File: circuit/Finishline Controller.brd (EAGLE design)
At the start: 101.6 x 53.3 mm, 8 parts

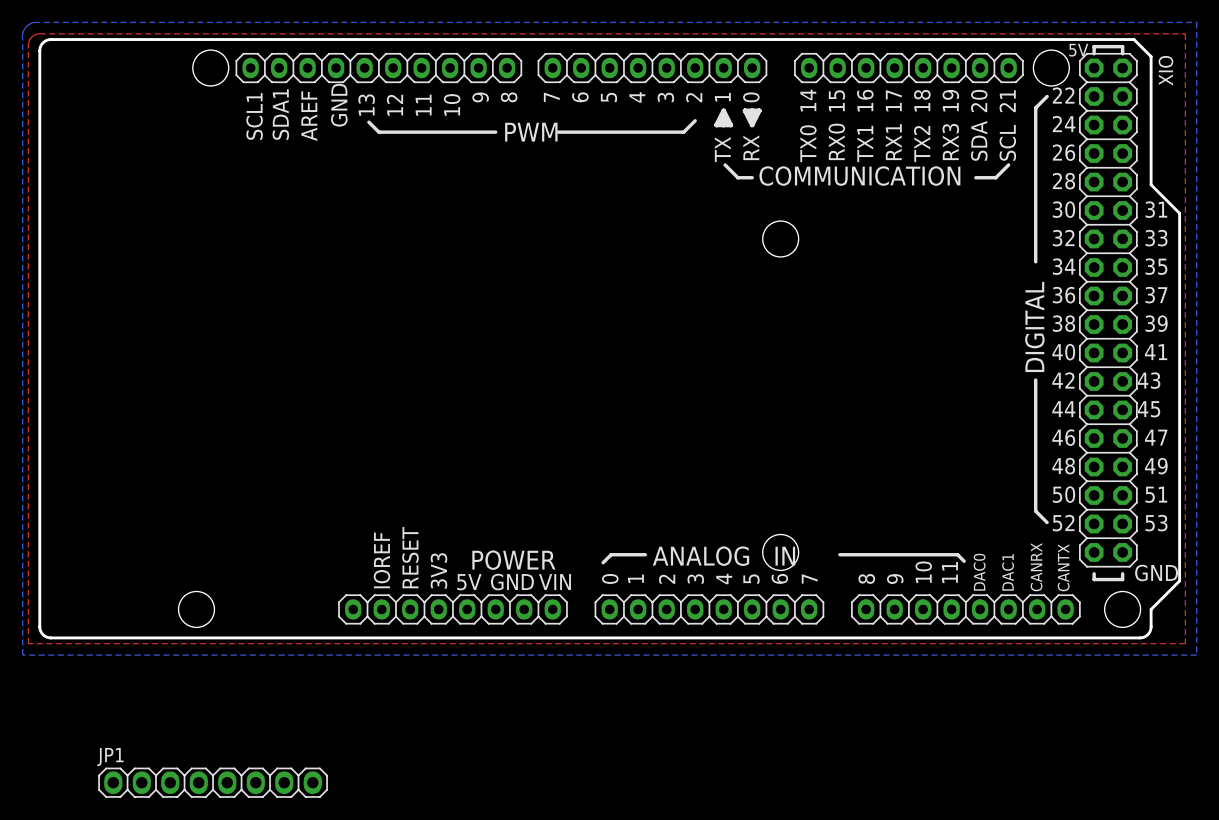
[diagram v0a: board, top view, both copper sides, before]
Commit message: add preliminary Due shield
The Due shield has been populated with all components to drive the
display as well as communicate with the start gate electronics.
A prototyping area with THT and SMD pads has been added as well.
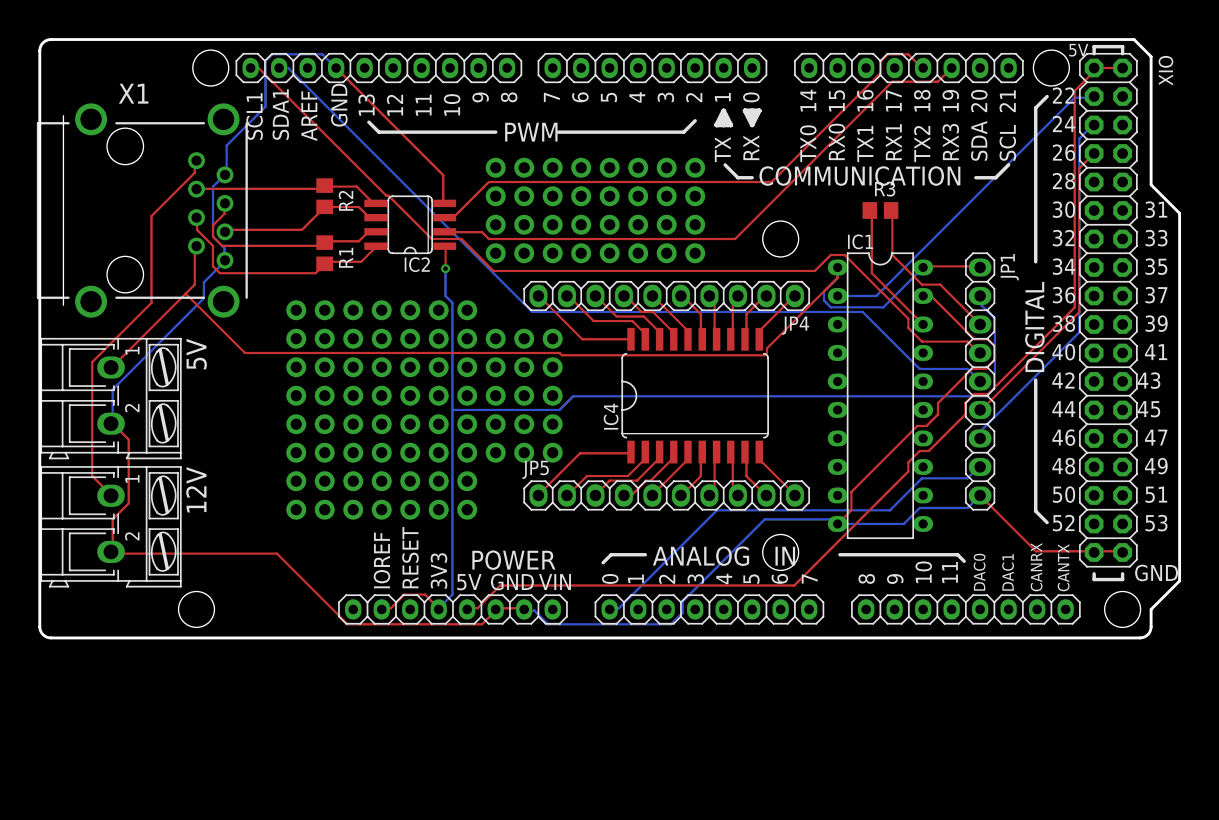
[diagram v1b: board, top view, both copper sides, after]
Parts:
- added 12V: 12V, con-ptr500:AK300/2
- added 5V: 5V, con-ptr500:AK300/2
- added IC1: 74HCT245N, 74xx-eu:DIL20
- added IC2: MAX3490ESA, miro:SO08
- added IC4: 74HCT245DW, 74xx-eu:SO20W
- added JP4, JP5: (no value), pinhead:1X10
- added R1, R2: 120, resistor:R0805
- added R3: 330, resistor:R0805
- added X1: RJ45-6LC21-B, con-tycoelectronics:RJ45-SHIELD1
- JP1: device pinhead:1X08 -> pinhead:1X09
- moved JP1 77.2 mm to (83.8, 22.9), turned to 270 degrees
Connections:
- removed net +3V3: POWER.2, POWER.4
- removed net +5V1: JP1.1
- removed net 0V: JP1.8
- removed net 3.3V: JP1.2
- removed net CLK: JP1.6
- removed net DIO: JP1.7
- removed net SCL: JP1.4
- removed net SDA: JP1.5
- new net +12VEXT: 12V.1, X1.1
- new net +3.3V: IC2.1, JP1.2, POWER.2, POWER.4
- new net +5VEXT: 5V.1, IC1.1, IC1.20, JP1.1, X1.7
- new net N$2: IC1.18, R3.1
- new net N$3: IC2.7, R1.1, X1.4
- new net N$4: IC2.6, R2.2, X1.6
- new net N$5: IC2.5, R2.1, X1.3
- new net N$6: IC2.8, R1.2, X1.5
- new net N$79: IC4.2, JP5.2
- new net N$80: IC4.3, JP5.3
- new net N$81: IC4.4, JP5.4
- new net N$82: IC4.5, JP5.5
- new net N$83: IC4.6, JP5.6
- new net N$84: IC4.7, JP5.7
- new net N$85: IC4.8, JP5.8
- new net N$86: IC4.9, JP5.9
- new net N$87: IC4.10, JP5.10
- new net N$88: IC4.1, JP5.1
- new net N$89: IC4.18, JP4.8
- new net N$90: IC4.17, JP4.7
- new net N$91: IC4.16, JP4.6
- new net N$92: IC4.15, JP4.5
- new net N$93: IC4.14, JP4.4
- new net N$94: IC4.13, JP4.3
- new net N$95: IC4.12, JP4.2
- new net N$96: IC4.11, JP4.1
- new net N$97: IC4.19, JP4.9
- new net N$98: IC4.20, JP4.10
- net AD0: now also JP1.8
- net GND: now also 12V.2, 5V.2, IC1.10, IC1.19, IC2.4, JP1.9, X1.2, X1.8
- net PIN22: now also IC1.2
- net PIN24: now also JP1.7
- net PIN26: now also JP1.6
- net RXD2: now also IC2.2
- net SCL1: now also JP1.4
- net SDA1: now also JP1.5
- net TXD2: now also IC2.3
- net WS2812DATA: now also R3.2
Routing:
- net GND: track 0.00 -> 208.2 mm
- net +5VEXT: track 0.00 -> 97.6 mm
- net +3.3V: track 0.00 -> 97.4 mm, vias 0 -> 1
- net +5V: track 0.00 -> 91.0 mm
- net SCL1: track 0.00 -> 77.2 mm
- net SDA1: track 0.00 -> 74.1 mm
- net RXD2: track 0.00 -> 51.8 mm
- net TXD2: track 0.00 -> 49.8 mm
- net AD0: track 0.00 -> 38.3 mm
- net +12VEXT: track 0.00 -> 34.4 mm
- net PIN24: track 0.00 -> 32.2 mm
- net PIN22: track 0.00 -> 30.2 mm
- net PIN26: track 0.00 -> 27.1 mm
- net N$6: track 0.00 -> 20.9 mm
- net N$3: track 0.00 -> 18.9 mm
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- removed copper zone on layer 1, net GND
- removed copper zone on layer 16, net GND

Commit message: add mounting holes to the Finishline Display board
New PDFs have been added for the display.
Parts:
- renumbered IC4 to PROTOTYPE
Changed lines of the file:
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@@
 <layer number="42" name="bRestrict" color="1" fill="10" visible="yes" active="yes"/>
 <layer number="43" name="vRestrict" color="2" fill="10" visible="yes" active="yes"/>
-<layer number="44" name="Drills" color="7" fill="1" visible="no" active="yes"/>
+<layer number="44" name="Drills" color="7" fill="1" visible="yes" active="yes"/>
 <layer number="45" name="Holes" color="7" fill="1" visible="yes" active="yes"/>
 <layer number="46" name="Milling" color="3" fill="1" visible="no" active="yes"/>
@@
 <layer number="112" name="tSilk" color="7" fill="1" visible="no" active="no"/>
 <layer number="113" name="ReferenceLS" color="7" fill="1" visible="no" active="no"/>
-<layer number="114" name="Badge_Outline" color="7" fill="1" visible="yes" active="yes"/>
-<layer number="115" name="ReferenceISLANDS" color="7" fill="1" visible="yes" active="yes"/>
+<layer number="114" name="Badge_Outline" color="7" fill="1" visible="no" active="yes"/>
+<layer number="115" name="ReferenceISLANDS" color="7" fill="1" visible="no" active="yes"/>
 <layer number="116" name="Patch_BOT" color="7" fill="1" visible="no" active="no"/>
 <layer number="118" name="Rect_Pads" color="7" fill="1" visible="no" active="no"/>
@@
 <layer number="127" name="_tValues" color="7" fill="1" visible="no" active="no"/>
 <layer number="128" name="_bValues" color="7" fill="1" visible="no" active="no"/>
-<layer number="129" name="Mask" color="7" fill="1" visible="yes" active="yes"/>
+<layer number="129" name="Mask" color="7" fill="1" visible="no" active="yes"/>
 <layer number="131" name="tAdjust" color="7" fill="1" visible="no" active="no"/>
 <layer number="132" name="bAdjust" color="7" fill="1" visible="no" active="no"/>
@@
 <layer number="223" name="223bmp" color="24" fill="1" visible="no" active="no"/>
 <layer number="224" name="224bmp" color="25" fill="1" visible="no" active="no"/>
-<layer number="225" name="225bmp" color="7" fill="1" visible="yes" active="yes"/>
-<layer number="226" name="226bmp" color="7" fill="1" visible="yes" active="yes"/>
-<layer number="227" name="227bmp" color="7" fill="1" visible="yes" active="yes"/>
-<layer number="228" name="228bmp" color="7" fill="1" visible="yes" active="yes"/>
-<layer number="229" name="229bmp" color="7" fill="1" visible="yes" active="yes"/>
-<layer number="230" name="230bmp" color="7" fill="1" visible="yes" active="yes"/>
+<layer number="225" name="225bmp" color="7" fill="1" visible="no" active="yes"/>
+<layer number="226" name="226bmp" color="7" fill="1" visible="no" active="yes"/>
+<layer number="227" name="227bmp" color="7" fill="1" visible="no" active="yes"/>
+<layer number="228" name="228bmp" color="7" fill="1" visible="no" active="yes"/>
+<layer number="229" name="229bmp" color="7" fill="1" visible="no" active="yes"/>
+<layer number="230" name="230bmp" color="7" fill="1" visible="no" active="yes"/>
 <layer number="231" name="Eagle3D_PG1" color="7" fill="1" visible="no" active="no"/>
 <layer number="232" name="Eagle3D_PG2" color="7" fill="1" visible="no" active="no"/>
@@
 <layer number="251" name="SMDround" color="12" fill="11" visible="no" active="no"/>
 <layer number="254" name="OrgLBR" color="13" fill="1" visible="no" active="no"/>
-<layer number="255" name="routoute" color="7" fill="1" visible="yes" active="yes"/>
+<layer number="255" name="routoute" color="7" fill="1" visible="no" active="yes"/>
 </layers>
 <board>
@@
 </element>
 <element name="R3" library="resistor" package="R0805" value="330" x="74.93" y="38.1"/>
-<element name="IC4" library="74xx-eu" package="SO20W" value="74HCT245DW" x="58.42" y="21.59"/>
+<element name="PROTOTYPE" library="74xx-eu" package="SO20W" value="74HCT245DW" x="58.42" y="21.59"/>
 <element name="JP4" library="pinhead" package="1X10" value="" x="55.88" y="30.48" rot="R180"/>
 <element name="JP5" library="pinhead" package="1X10" value="" x="55.88" y="12.7"/>
@@
 <signal name="N$79">
 <contactref element="JP5" pad="2"/>
-<contactref element="IC4" pad="2"/>
+<contactref element="PROTOTYPE" pad="2"/>
 <wire x1="53.848" y1="15.8496" x2="53.848" y2="16.4592" width="0.2032" layer="1"/>
 <wire x1="52.4256" y1="14.4272" x2="53.848" y2="15.8496" width="0.2032" layer="1"/>
@@
 <signal name="N$80">
 <contactref element="JP5" pad="3"/>
-<contactref element="IC4" pad="3"/>
+<contactref element="PROTOTYPE" pad="3"/>
 <wire x1="55.0672" y1="15.8496" x2="55.0672" y2="16.4592" width="0.2032" layer="1"/>
 <wire x1="53.2384" y1="14.0208" x2="55.0672" y2="15.8496" width="0.2032" layer="1"/>
@@
 <signal name="N$81">
 <contactref element="JP5" pad="4"/>
-<contactref element="IC4" pad="4"/>
+<contactref element="PROTOTYPE" pad="4"/>
 <wire x1="56.4896" y1="16.0528" x2="56.4896" y2="16.4592" width="0.2032" layer="1"/>
 <wire x1="54.4576" y1="14.0208" x2="56.4896" y2="16.0528" width="0.2032" layer="1"/>
@@
 <signal name="N$82">
 <contactref element="JP5" pad="5"/>
-<contactref element="IC4" pad="5"/>
+<contactref element="PROTOTYPE" pad="5"/>
 <wire x1="57.7088" y1="15.8496" x2="57.7088" y2="16.4592" width="0.2032" layer="1"/>
 <wire x1="54.6608" y1="12.8016" x2="57.7088" y2="15.8496" width="0.2032" layer="1"/>
@@
 <signal name="N$83">
 <contactref element="JP5" pad="6"/>
-<contactref element="IC4" pad="6"/>
+<contactref element="PROTOTYPE" pad="6"/>
 <wire x1="58.928" y1="14.4272" x2="58.928" y2="16.4592" width="0.2032" layer="1"/>
 <wire x1="57.3024" y1="12.8016" x2="58.928" y2="14.4272" width="0.2032" layer="1"/>
@@
 <signal name="N$84">
 <contactref element="JP5" pad="7"/>
-<contactref element="IC4" pad="7"/>
+<contactref element="PROTOTYPE" pad="7"/>
 <wire x1="60.1472" y1="13.208" x2="60.1472" y2="16.4592" width="0.2032" layer="1"/>
 <wire x1="59.7408" y1="12.8016" x2="60.1472" y2="13.208" width="0.2032" layer="1"/>
@@
 <signal name="N$85">
 <contactref element="JP5" pad="8"/>
-<contactref element="IC4" pad="8"/>
+<contactref element="PROTOTYPE" pad="8"/>
 <wire x1="61.7728" y1="13.208" x2="61.7728" y2="16.4592" width="0.2032" layer="1"/>
 <wire x1="62.1792" y1="12.8016" x2="61.7728" y2="13.208" width="0.2032" layer="1"/>
@@
 <signal name="N$86">
 <contactref element="JP5" pad="9"/>
-<contactref element="IC4" pad="9"/>
+<contactref element="PROTOTYPE" pad="9"/>
 <wire x1="62.992" y1="14.4272" x2="62.992" y2="16.4592" width="0.2032" layer="1"/>
 <wire x1="64.6176" y1="12.8016" x2="62.992" y2="14.4272" width="0.2032" layer="1"/>
@@
 <signal name="N$87">
 <contactref element="JP5" pad="10"/>
-<contactref element="IC4" pad="10"/>
+<contactref element="PROTOTYPE" pad="10"/>
 <wire x1="64.2112" y1="15.8496" x2="64.2112" y2="16.4592" width="0.2032" layer="1"/>
 <wire x1="67.2592" y1="12.8016" x2="64.2112" y2="15.8496" width="0.2032" layer="1"/>
@@
 </signal>
 <signal name="N$88">
-<contactref element="IC4" pad="1"/>
+<contactref element="PROTOTYPE" pad="1"/>
 <contactref element="JP5" pad="1"/>
 <wire x1="48.1584" y1="16.4592" x2="52.6288" y2="16.4592" width="0.2032" layer="1"/>
@@
 </signal>
 <signal name="N$89">
-<contactref element="IC4" pad="18"/>
+<contactref element="PROTOTYPE" pad="18"/>
 <contactref element="JP4" pad="8"/>
 <wire x1="55.0672" y1="27.432" x2="55.0672" y2="26.6192" width="0.2032" layer="1"/>
@@
 </signal>
 <signal name="N$90">
-<contactref element="IC4" pad="17"/>
+<contactref element="PROTOTYPE" pad="17"/>
 <contactref element="JP4" pad="7"/>
 <wire x1="56.4896" y1="27.2288" x2="56.4896" y2="26.6192" width="0.2032" layer="1"/>
@@
 <signal name="N$91">
 <contactref element="JP4" pad="6"/>
-<contactref element="IC4" pad="16"/>
+<contactref element="PROTOTYPE" pad="16"/>
 <wire x1="57.7088" y1="27.432" x2="57.7088" y2="26.6192" width="0.2032" layer="1"/>
 <wire x1="54.6608" y1="30.48" x2="57.7088" y2="27.432" width="0.2032" layer="1"/>
@@
 <signal name="N$92">
 <contactref element="JP4" pad="5"/>
-<contactref element="IC4" pad="15"/>
+<contactref element="PROTOTYPE" pad="15"/>
 <wire x1="58.928" y1="28.8544" x2="58.928" y2="26.6192" width="0.2032" layer="1"/>
 <wire x1="57.3024" y1="30.48" x2="58.928" y2="28.8544" width="0.2032" layer="1"/>
@@
 <signal name="N$93">
 <contactref element="JP4" pad="4"/>
-<contactref element="IC4" pad="14"/>
+<contactref element="PROTOTYPE" pad="14"/>
 <wire x1="60.1472" y1="30.0736" x2="60.1472" y2="26.6192" width="0.2032" layer="1"/>
 <wire x1="59.7408" y1="30.48" x2="60.1472" y2="30.0736" width="0.2032" layer="1"/>
@@
 <signal name="N$94">
 <contactref element="JP4" pad="3"/>
-<contactref element="IC4" pad="13"/>
+<contactref element="PROTOTYPE" pad="13"/>
 <wire x1="61.7728" y1="30.0736" x2="61.7728" y2="26.6192" width="0.2032" layer="1"/>
 <wire x1="62.1792" y1="30.48" x2="61.7728" y2="30.0736" width="0.2032" layer="1"/>
@@
 <signal name="N$95">
 <contactref element="JP4" pad="2"/>
-<contactref element="IC4" pad="12"/>
+<contactref element="PROTOTYPE" pad="12"/>
 <wire x1="62.992" y1="28.8544" x2="62.992" y2="26.6192" width="0.2032" layer="1"/>
 <wire x1="64.6176" y1="30.48" x2="62.992" y2="28.8544" width="0.2032" layer="1"/>
@@
 <signal name="N$96">
 <contactref element="JP4" pad="1"/>
-<contactref element="IC4" pad="11"/>
+<contactref element="PROTOTYPE" pad="11"/>
 <wire x1="64.2112" y1="27.432" x2="64.2112" y2="26.6192" width="0.2032" layer="1"/>
 <wire x1="67.2592" y1="30.48" x2="64.2112" y2="27.432" width="0.2032" layer="1"/>
@@
 </signal>
 <signal name="N$97">
-<contactref element="IC4" pad="19"/>
+<contactref element="PROTOTYPE" pad="19"/>
 <contactref element="JP4" pad="9"/>
 <wire x1="53.848" y1="27.2288" x2="53.848" y2="26.6192" width="0.2032" layer="1"/>
@@
 </signal>
 <signal name="N$98">
-<contactref element="IC4" pad="20"/>
+<contactref element="PROTOTYPE" pad="20"/>
 <contactref element="JP4" pad="10"/>
 <wire x1="48.3616" y1="26.6192" x2="52.705" y2="26.6192" width="0.2032" layer="1"/>

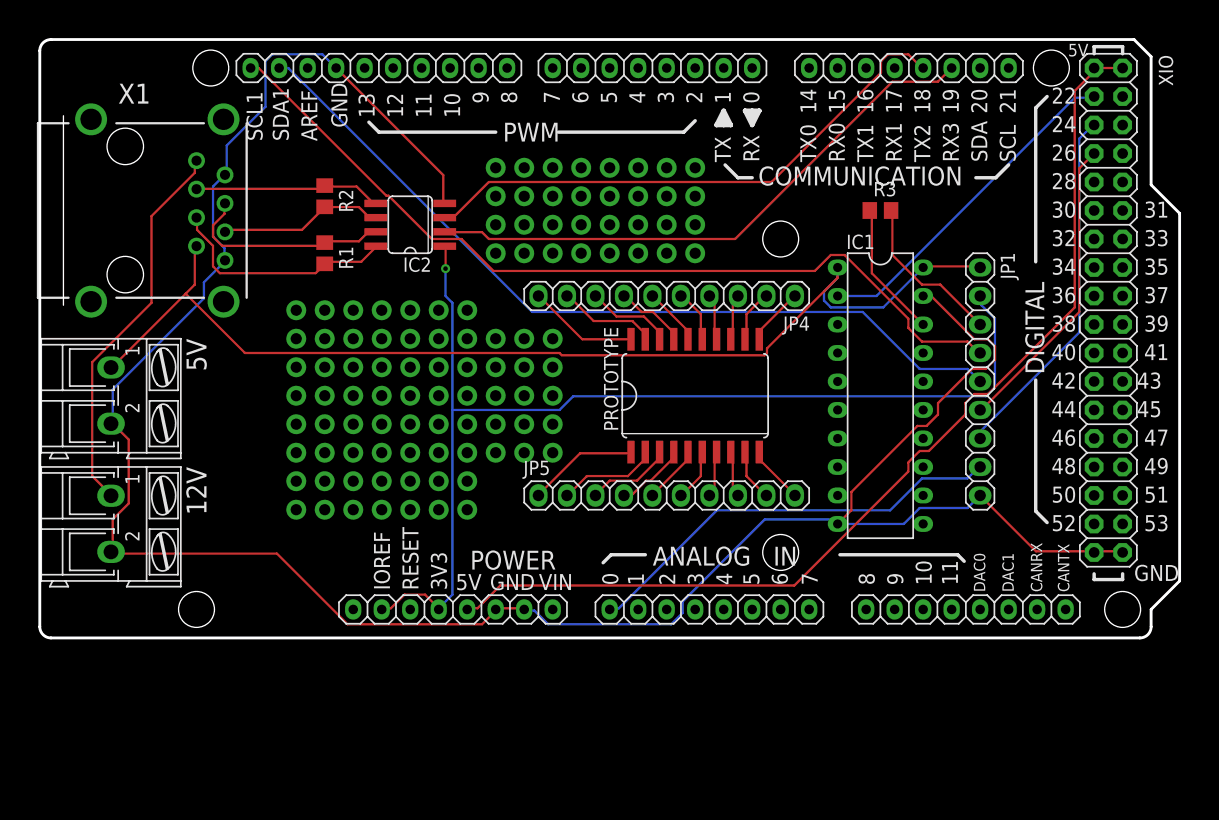
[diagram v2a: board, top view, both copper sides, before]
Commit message: finalize display module and controller shield
Display Module: Reordered the WS2813 LEDs to be consistent with normal
7-segment LED numbers (a-g). Changed schematics to be in the same
orientation as the board in top view. Re-adds the capacitors for the
WS2812 LEDs and the LDR line, which inadvertently got lost in the last
commit. Added silk screen.

Controller Shield: Added large electrolyte capacitor to buffer for the
WS2812 LEDs. Added a series resistor for the WS2812 data line. Added
silk screen and corrected wrong pinout of the I2C and serial header.
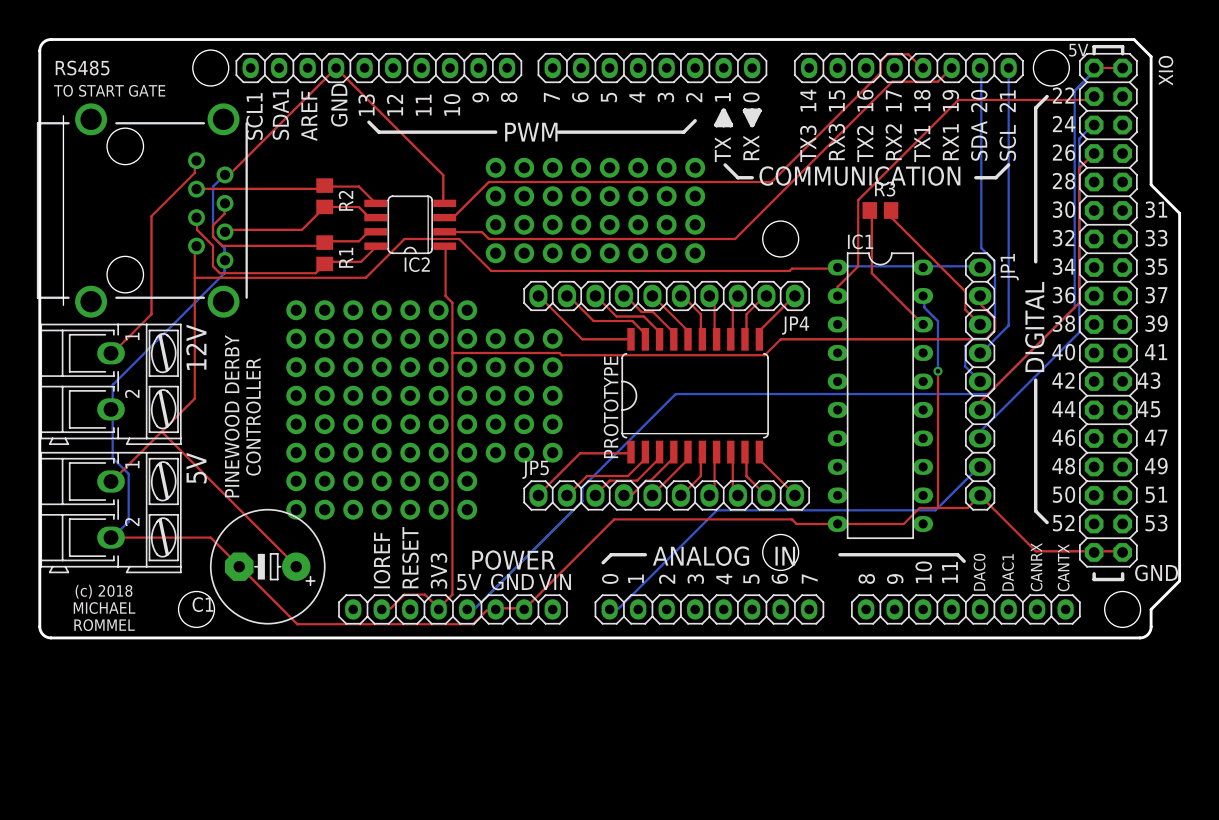
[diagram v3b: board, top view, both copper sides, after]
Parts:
- added C1: (no value), resistor:E5-10,5
- moved 12V 12.7 mm to (6.35, 22.9)
- moved 5V 10.2 mm to (6.35, 11.4)
- renumbered X1 to RS485
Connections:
- net RXD0 renamed RX3
- net RXD1 renamed RX2
- net RXD2 renamed RX1
- net TXD0 renamed TX3
- net TXD1 renamed TX2
- net TXD2 renamed TX1
- removed net SCL0-3: COMMUNICATION.8
- removed net SDA0-3: COMMUNICATION.7
- new net SCL0: COMMUNICATION.8, JP1.4
- new net SDA0: COMMUNICATION.7, JP1.5
- net +5VEXT: now also C1.+
- net GND: now also C1.-
- net SCL1: no longer JP1.4
- net SDA1: no longer JP1.5
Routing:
- net SCL1: track 77.2 -> 0.00 mm
- net SDA1: track 74.1 -> 0.00 mm
- net SDA0: track 0.00 -> 30.9 mm
- net SCL0: track 0.00 -> 26.5 mm
- net GND: track 208.2 -> 189.2 mm, vias 0 -> 1
- net +5VEXT: track 97.6 -> 114.2 mm
- net +12VEXT: track 34.4 -> 20.4 mm
- net +3.3V: track 97.4 -> 92.4 mm, vias 1 -> 0
- net PIN22: track 30.2 -> 34.2 mm
- net WS2812DATA: track 14.4 -> 13.5 mm
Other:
- board text added: "(c) 2018 MICHAEL ROMMEL"
- board text added: "PINEWOOD DERBY CONTROLLER"
- board text added: "RX2"
- board text added: "TO START GATE"
- board text added: "TX3"
- board text removed: "RX0"
- board text removed: "TX0"
